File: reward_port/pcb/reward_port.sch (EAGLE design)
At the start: 16 parts, among them U2 ATTINY2313A

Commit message: more schematic layout
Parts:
- removed S3: SWITCH-MOMENTARY-2SMD-4, SparkFun-Electromechanical:SWITCH-MOMENTARY-2SMD-4
- added R1: 10K, SparkFun-Resistors:10KOHM-1/10W-1%(0603)0603
- added RESET: SWITCH-MOMENTARY-2SMD-4, SparkFun-Electromechanical:SWITCH-MOMENTARY-2SMD-4
- added U$5: 4-POS-DIP, SparkFun-Electromechanical:4-POS-DIP
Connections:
- net +3V6 renamed N$10
- removed net N$5: C1.-, U$3.GND
- new net 12V: C1.+, U$2.IN, U$3.VMOT
- new net DIR: U$3.DIR
- new net N$11: U$3.MS1, U$5.1A
- new net N$12: U$3.MS2, U$5.2A
- new net N$13: U$3.MS3, U$5.3A
- new net N$14: U$1.7, U2.PB7/SCK/SCL
- new net N$15: U$1.9, U2.PB6/MISO/DO
- new net N$16: U$1.1, U2.PB5/MOSI/SDA/DI
- new net STEP: U$3.STEP
- new net VDD33: R1.2, U$1.2, U$2.OUT, U$3.VDD, U$5.1B, U$5.2B, U$5.3B, U$5.4B, U2.VCC
- net GND: now also C1.-, RESET.1, U$1.10, U$1.4, U$1.6, U$1.8, U$2.GND, U$3.GND, U2.GND
- net N$4: now also R1.1, RESET.2, U$1.5, U2.PA2/!RESET; no longer C1.+, U$3.VMOT
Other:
- moved on the sheet: C1, J1, J2, U$1, U$2, U2

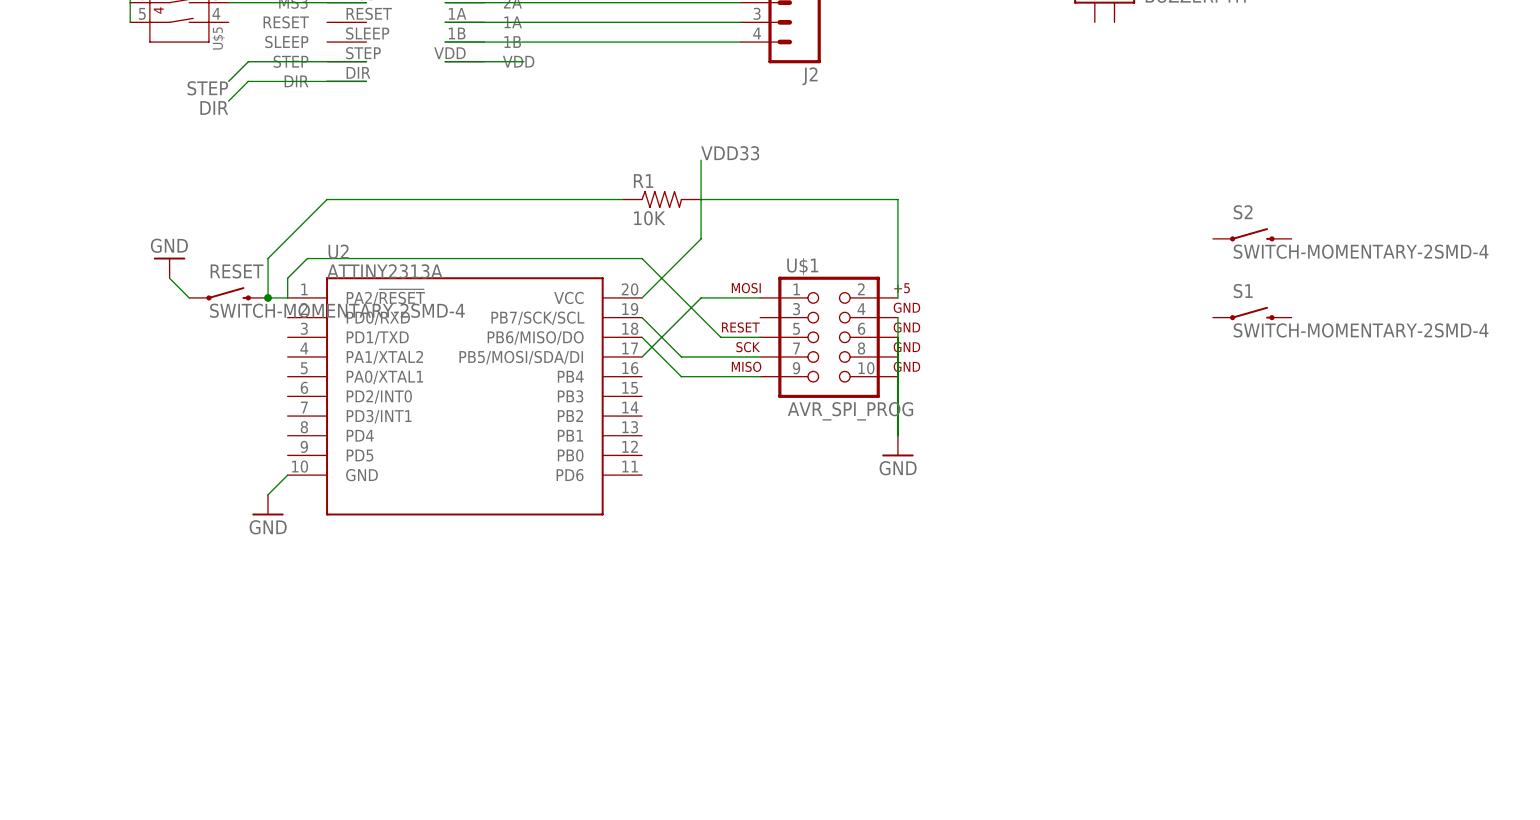
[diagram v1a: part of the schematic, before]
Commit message: replaced micro controller with attiny84
needed Ain for LED thresholding
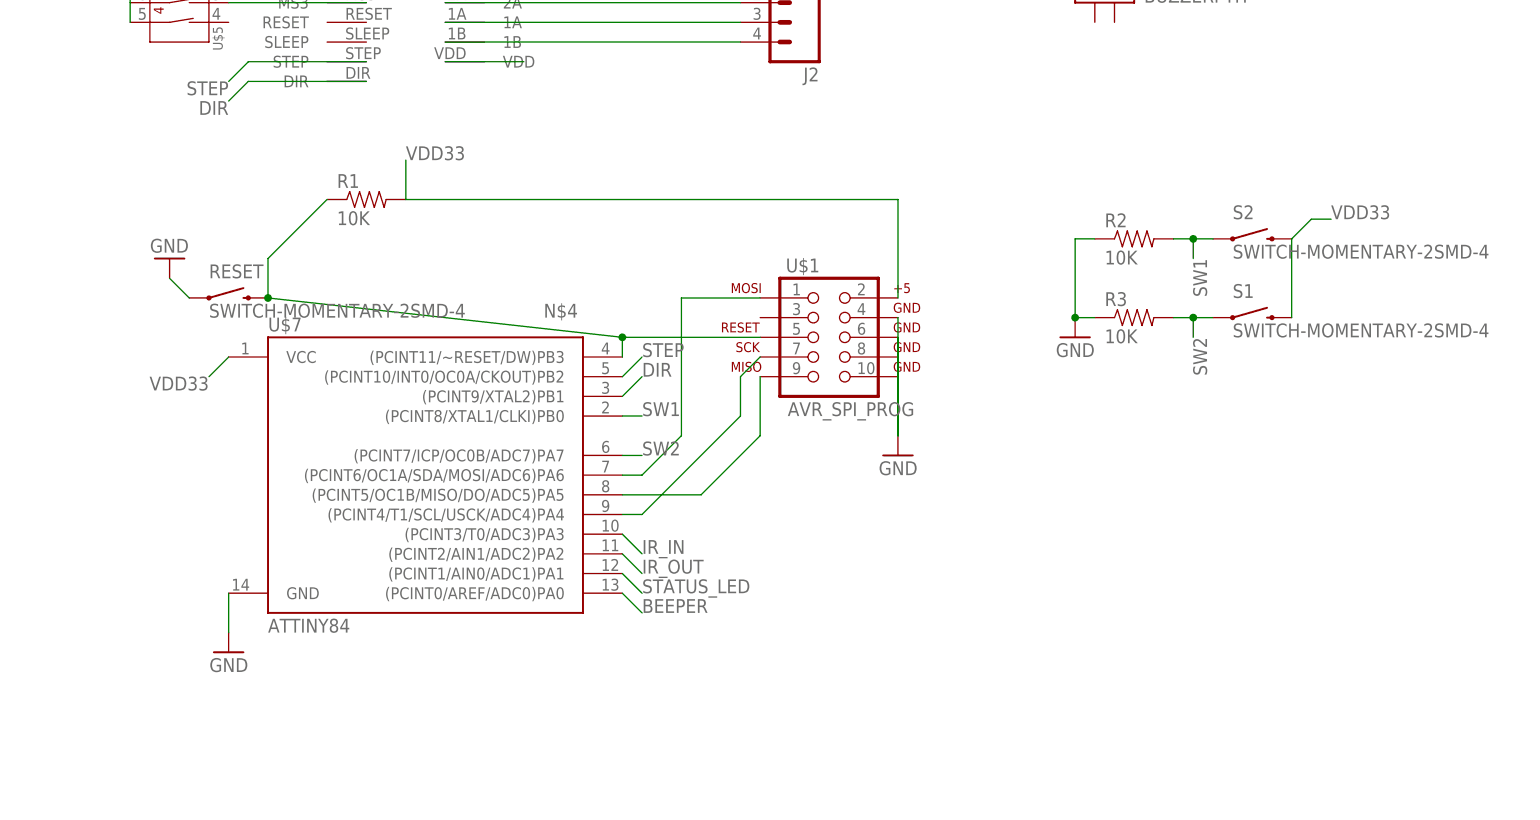
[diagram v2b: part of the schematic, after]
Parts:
- removed U2: ATTINY2313A, SparkFun-DigitalIC:ATTINY2313A
- added R2, R3: 10K, SparkFun-Resistors:10KOHM-1/10W-1%(0603)0603
- added U$7: ATTINY84, SparkFun-DigitalIC:ATTINY84
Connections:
- removed net N$15: U$1.9, U2.PB6/MISO/DO
- new net BEEPER: U$7.(PCINT0/AREF/ADC0)PA0
- new net IR_IN: U$7.(PCINT3/T0/ADC3)PA3
- new net IR_OUT: U$7.(PCINT2/AIN1/ADC2)PA2
- new net N$5: U$1.9, U$7.(PCINT5/OC1B/MISO/DO/ADC5)PA5
- new net STATUS_LED: U$7.(PCINT1/AIN0/ADC1)PA1
- new net SW1: R2.2, S2.1, U$7.(PCINT8/XTAL1/CLKI)PB0
- new net SW2: R3.2, S1.1, U$7.(PCINT7/ICP/OC0B/ADC7)PA7
- net DIR: now also U$7.(PCINT9/XTAL2)PB1
- net GND: now also R2.1, R3.1, U$7.GND; no longer U2.GND
- net N$14: now also U$7.(PCINT4/T1/SCL/USCK/ADC4)PA4; no longer U2.PB7/SCK/SCL
- net N$16: now also U$7.(PCINT6/OC1A/SDA/MOSI/ADC6)PA6; no longer U2.PB5/MOSI/SDA/DI
- net N$4: now also U$7.(PCINT11/~RESET/DW)PB3; no longer U2.PA2/!RESET
- net STEP: now also U$7.(PCINT10/INT0/OC0A/CKOUT)PB2
- net VDD33: now also S1.2, S2.2, U$7.VCC; no longer U2.VCC
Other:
- moved on the sheet: R1

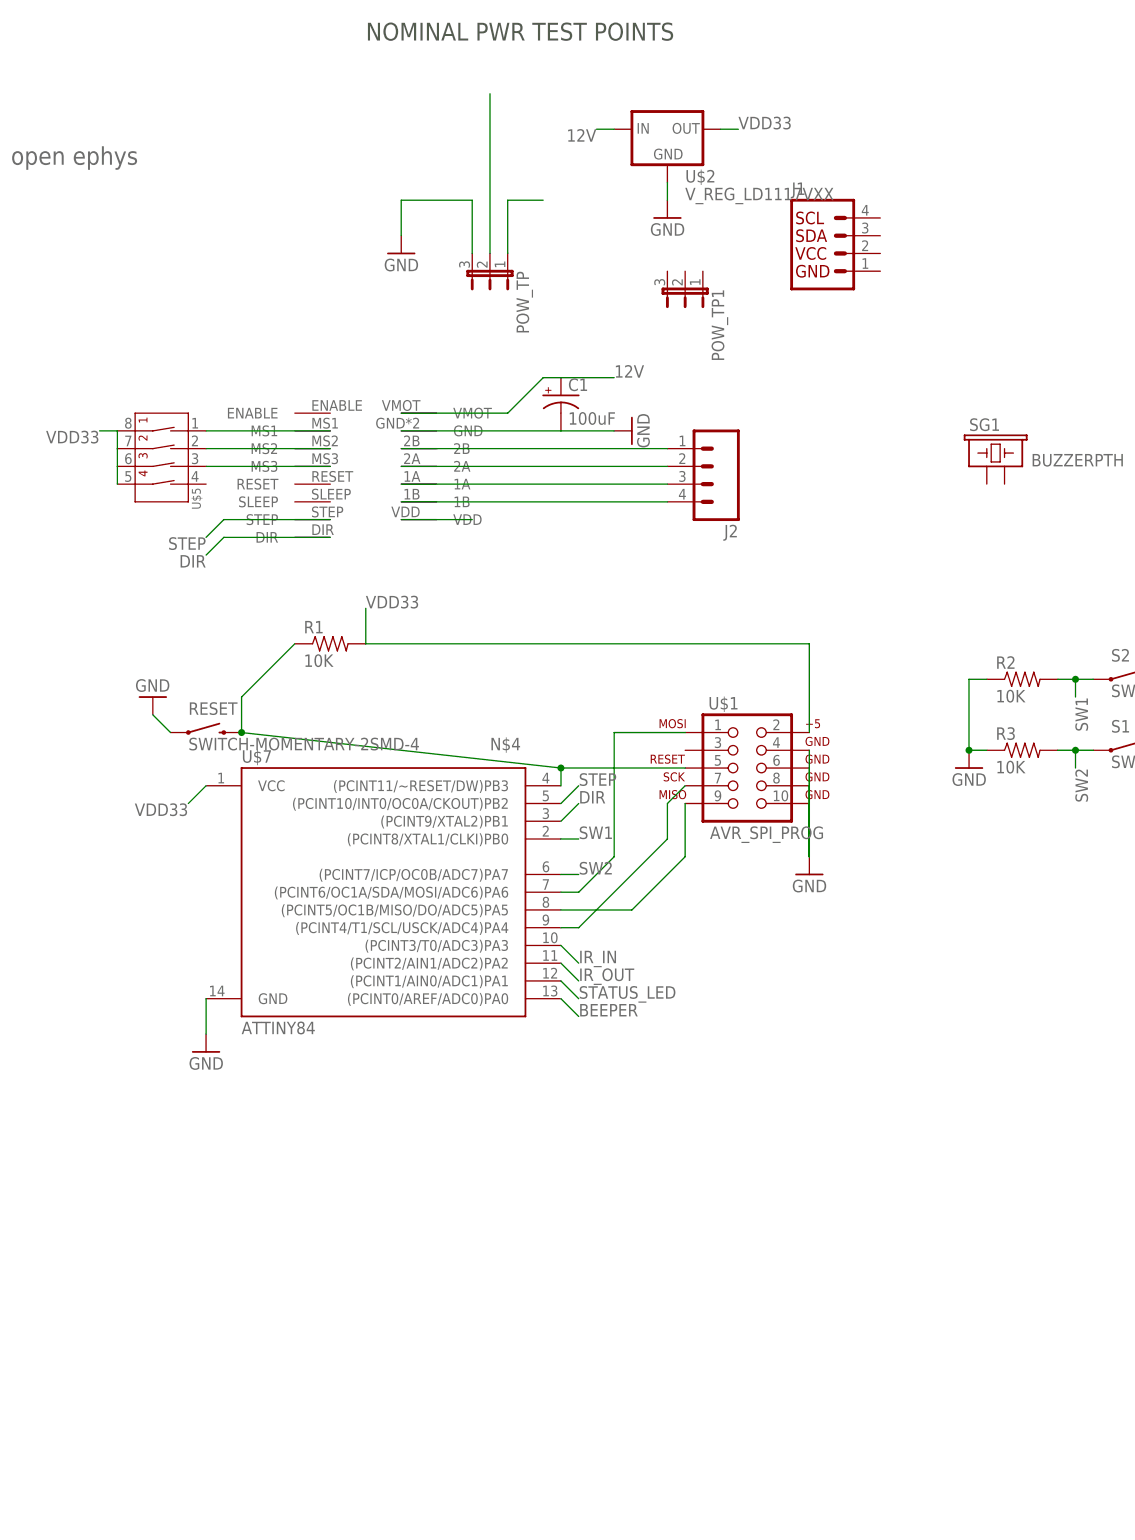
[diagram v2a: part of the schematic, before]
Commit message: went to atmega32 for i2c bus
at this point the price is getting close to a teensy per port
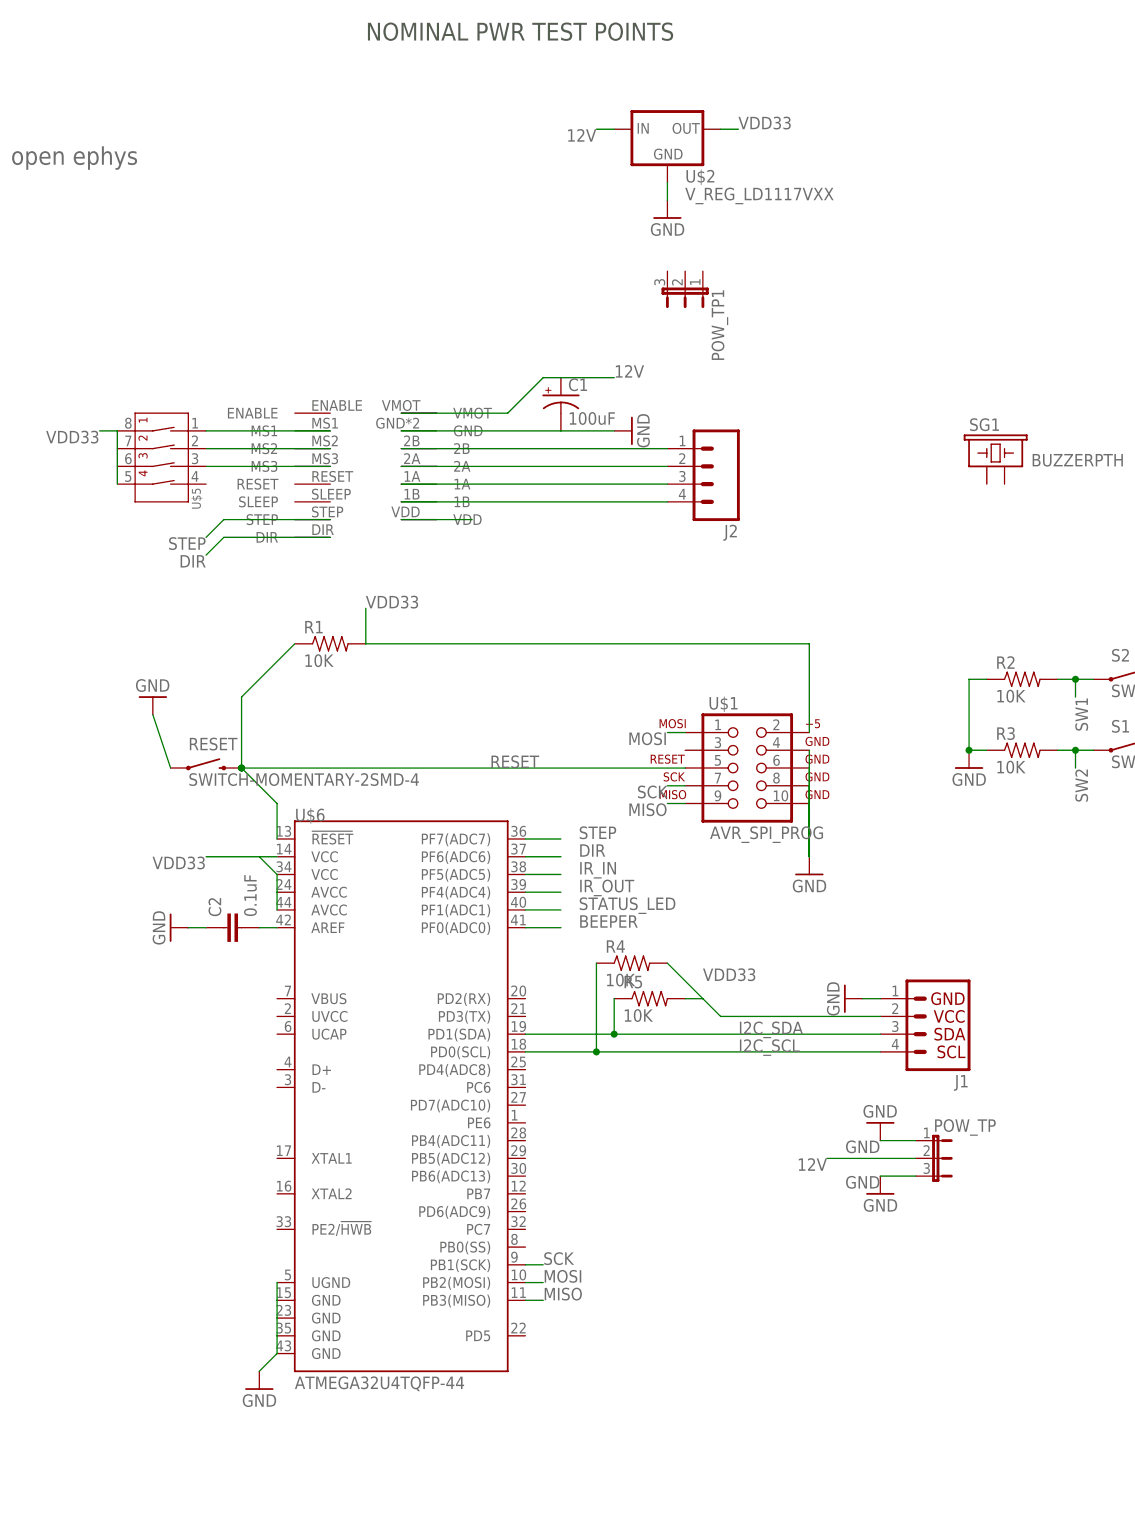
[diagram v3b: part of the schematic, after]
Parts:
- removed U$7: ATTINY84, SparkFun-DigitalIC:ATTINY84
- added C2: 0.1uF, SparkFun-Capacitors:0.1UF-25V(+80/-20%)(0603)
- added R4, R5: 10K, SparkFun-Resistors:10KOHM-1/10W-1%(0603)0603
- added U$6: ATMEGA32U4TQFP-44, SparkFun-DigitalIC:ATMEGA32U4TQFP-44
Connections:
- removed net N$10: POW_TP.2
- removed net N$14: U$1.7, U$7.(PCINT4/T1/SCL/USCK/ADC4)PA4
- removed net N$16: U$1.1, U$7.(PCINT6/OC1A/SDA/MOSI/ADC6)PA6
- removed net N$3: POW_TP.1
- removed net N$4: R1.1, RESET.2, U$1.5, U$7.(PCINT11/~RESET/DW)PB3
- removed net N$5: U$1.9, U$7.(PCINT5/OC1B/MISO/DO/ADC5)PA5
- new net I2C_SCL: J1.4, R4.1, U$6.PD0(SCL)
- new net I2C_SDA: J1.3, R5.1, U$6.PD1(SDA)
- new net MISO: U$1.9, U$6.PB3(MISO)
- new net MOSI: U$1.1, U$6.PB2(MOSI)
- new net N$15: C2.2, U$6.AREF
- new net RESET: R1.1, RESET.2, U$1.5, U$6.!RESET
- new net SCK: U$1.7, U$6.PB1(SCK)
- net 12V: now also POW_TP.2
- net BEEPER: now also U$6.PF0(ADC0); no longer U$7.(PCINT0/AREF/ADC0)PA0
- net DIR: now also U$6.PF6(ADC6); no longer U$7.(PCINT9/XTAL2)PB1
- net GND: now also C2.1, J1.1, POW_TP.1, U$6.GND@15, U$6.GND@23, U$6.GND@35, U$6.GND@43, U$6.UGND; no longer U$7.GND
- net IR_IN: now also U$6.PF5(ADC5); no longer U$7.(PCINT3/T0/ADC3)PA3
- net IR_OUT: now also U$6.PF4(ADC4); no longer U$7.(PCINT2/AIN1/ADC2)PA2
- net STATUS_LED: now also U$6.PF1(ADC1); no longer U$7.(PCINT1/AIN0/ADC1)PA1
- net STEP: now also U$6.PF7(ADC7); no longer U$7.(PCINT10/INT0/OC0A/CKOUT)PB2
- net SW1: no longer U$7.(PCINT8/XTAL1/CLKI)PB0
- net SW2: no longer U$7.(PCINT7/ICP/OC0B/ADC7)PA7
- net VDD33: now also J1.2, R4.2, R5.2, U$6.AVCC@24, U$6.AVCC@44, U$6.VCC@14, U$6.VCC@34; no longer U$7.VCC
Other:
- moved on the sheet: J1, POW_TP, RESET

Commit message: more layout and sch
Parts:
- removed D1, D2: (no value), SparkFun-LED:LED-3MM-NO_SILK
- removed J2: (no value), SparkFun-Connectors:M04JST
- removed U$4: OPEN_EPHYS_LOGO, open-ephys:OPEN_EPHYS_LOGO
- added C3: 10uF, SparkFun-Capacitors:10UF-6.3V-20%(0603)
- added C4: 0.1uF, SparkFun-Capacitors:0.1UF-25V-5%(0603)
- added DETECTOR, EMITTER: (no value), SparkFun-LED:LED-3MM-NO_SILK
- added J3: (no value), SparkFun-Connectors:M05X2PTH
- added J7: (no value), SparkFun-Connectors:M04POLAR
- added R6, R7: 100, SparkFun-Resistors:10KOHM-1/10W-1%(0603)0603
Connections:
- removed net VDD33: J1.2, R1.2, R4.2, R5.2, S1.2, S2.2, U$1.2, U$2.OUT, U$3.VDD, U$5.1B, U$5.2B, U$5.3B, U$5.4B, U$6.AVCC@24, U$6.AVCC@44, U$6.VCC@14, U$6.VCC@34
- new net N$20: J3.7, U$6.PB7
- new net N$21: EMITTER.C, R6.2
- new net N$22: J3.5, U$6.PB6(ADC13)
- new net N$23: J3.3, U$6.PB5(ADC12)
- new net N$24: J3.1, U$6.PB4(ADC11)
- new net N$25: J3.2, U$6.PE6
- new net N$26: J3.4, U$6.PD7(ADC10)
- new net N$27: J3.6, U$6.PC6
- new net N$3: J3.9, U$6.PD6(ADC9)
- new net VDD: C3.1, J1.2, J3.10, R1.2, R4.2, R5.2, R7.1, S1.2, S2.2, U$1.2, U$2.OUT, U$3.VDD, U$5.1B, U$5.2B, U$5.3B, U$5.4B, U$6.AVCC@24, U$6.AVCC@44, U$6.VCC@14, U$6.VCC@34
- net 12V: now also C4.1
- net BEEPER: now also SG1.2
- net GND: now also C3.2, C4.2, DETECTOR.C, J3.8, R6.1, SG1.1
- net IR_IN: now also DETECTOR.A, R7.2
- net IR_OUT: now also EMITTER.A
- net N$6: now also J7.1; no longer J2.1
- net N$7: now also J7.2; no longer J2.2
- net N$8: now also J7.3; no longer J2.3
- net N$9: now also J7.4; no longer J2.4
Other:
- note added: "select 5V or 3.3v, likely 5 is better"
- note removed: "NOMINAL PWR TEST POINTS"
